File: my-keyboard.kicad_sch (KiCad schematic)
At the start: 156 parts, among them SW1 SW_Push, U1 ATmega32U4-AU, Y1 16MHz

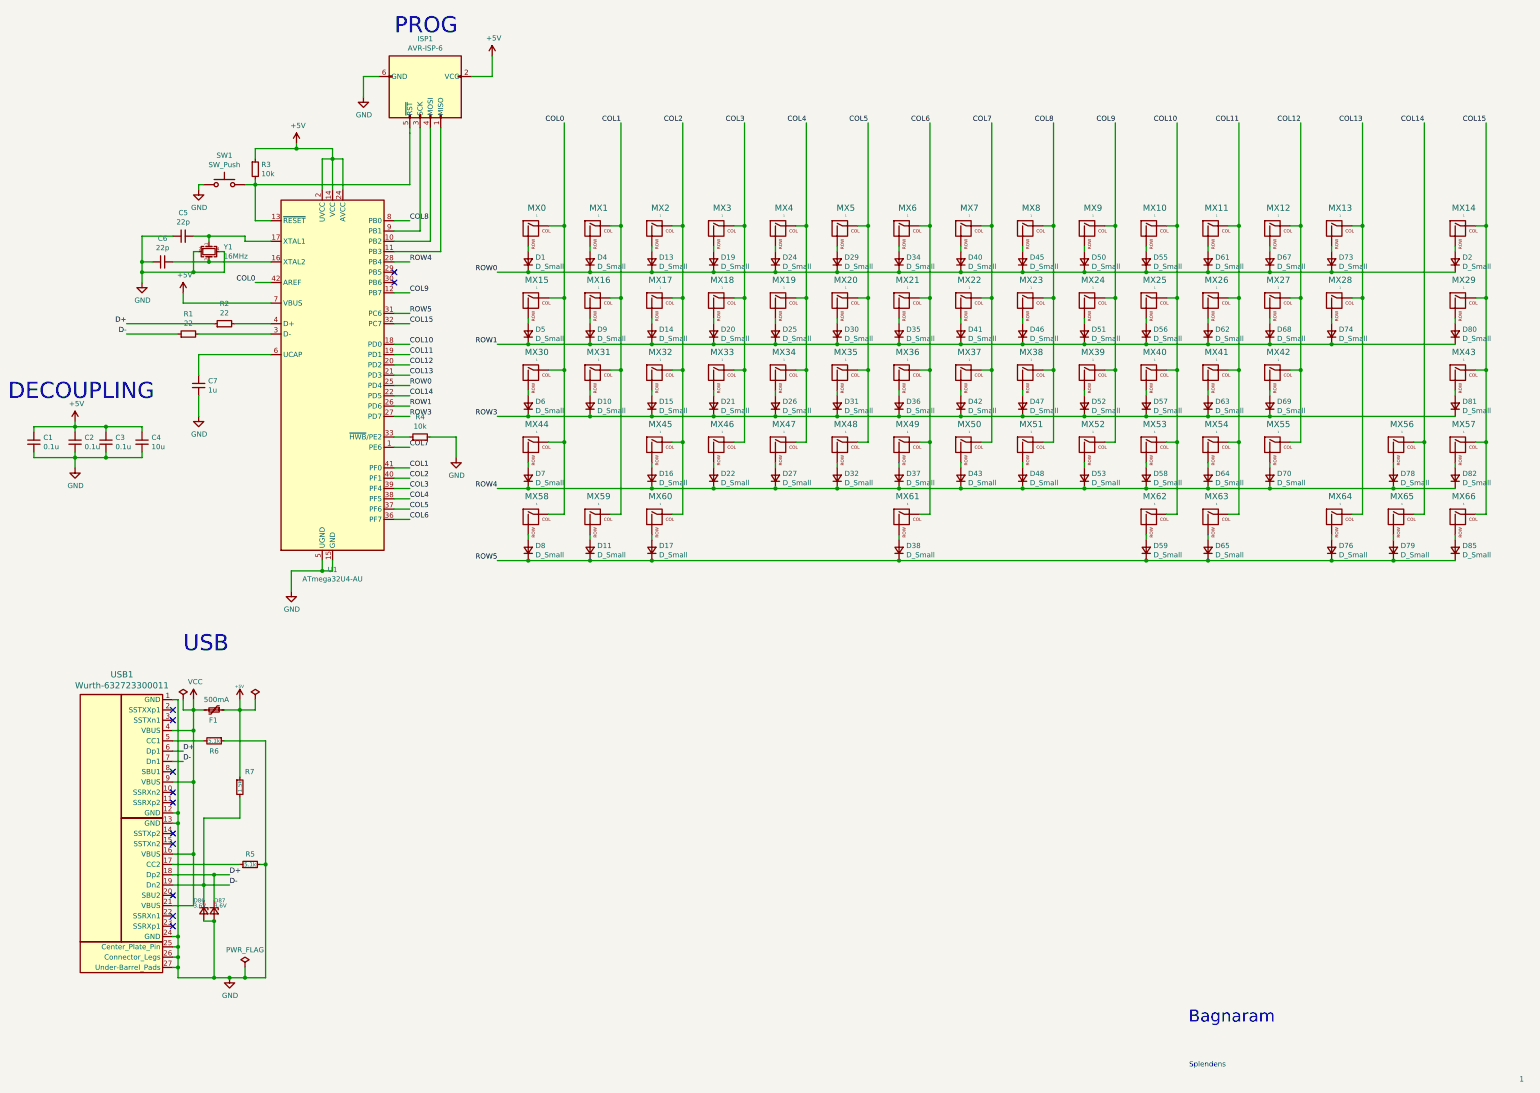
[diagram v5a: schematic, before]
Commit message: fix aref pin
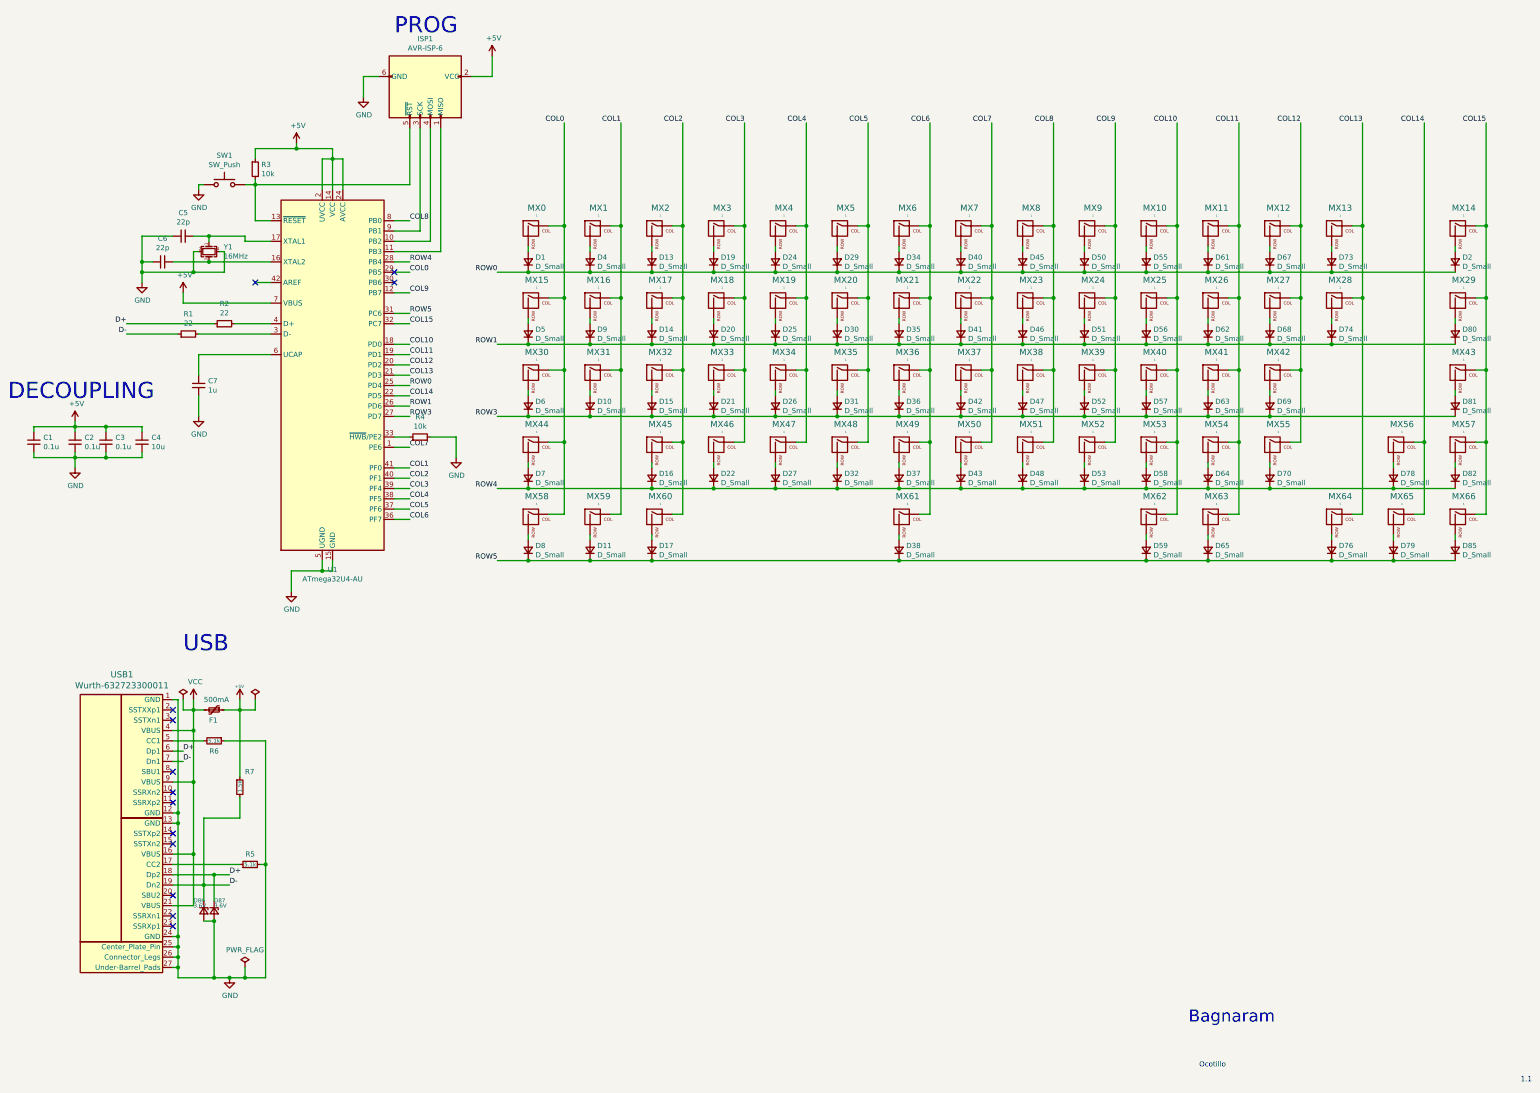
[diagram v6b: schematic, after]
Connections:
- net COL0: now also U1.29 (PB5); no longer U1.42 (AREF)
- no-connect marks 12 -> 13
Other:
- note added: "1.1"
- note added: "Ocotillo"
- note removed: "1"
- note removed: "Splendens"
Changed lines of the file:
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@@
   (junction (at 383.54 105.41) (diameter 1.016) (color 0 0 0 0))
   (junction (at 383.54 123.19) (diameter 1.016) (color 0 0 0 0))
-  (no_connect (at 59.69 234.95))
+  (no_connect (at 59.69 204.47))
   (no_connect (at 59.69 212.09))
-  (no_connect (at 59.69 219.71))
-  (no_connect (at 59.69 242.57))
-  (no_connect (at 59.69 191.77))
+  (no_connect (at 80.01 83.82))
   (no_connect (at 59.69 222.25))
   (no_connect (at 114.3 81.28))
-  (no_connect (at 59.69 204.47))
+  (no_connect (at 59.69 191.77))
+  (no_connect (at 59.69 219.71))
+  (no_connect (at 59.69 240.03))
+  (no_connect (at 59.69 242.57))
+  (no_connect (at 59.69 209.55))
+  (no_connect (at 59.69 234.95))
   (no_connect (at 59.69 189.23))
-  (no_connect (at 59.69 240.03))
   (no_connect (at 114.3 83.82))
-  (no_connect (at 59.69 209.55))
   (wire (pts (xy 25.4 119.38) (xy 25.4 120.65))
     (stroke (width 0) (type solid) (color 0 0 0 0))
@@
     (stroke (width 0) (type solid) (color 0 0 0 0))
   )
+  (wire (pts (xy 114.3 81.28) (xy 118.11 81.28))
+    (stroke (width 0) (type solid) (color 0 0 0 0))
+  )
   (wire (pts (xy 114.3 86.36) (xy 118.11 86.36))
     (stroke (width 0) (type solid) (color 0 0 0 0))
@@
     (stroke (width 0) (type solid) (color 0 0 0 0))
   )
-  (wire (pts (xy 118.11 46.99) (xy 118.11 45.72))
-    (stroke (width 0) (type solid) (color 0 0 0 0))
-  )
-  (wire (pts (xy 118.11 46.99) (xy 118.11 59.69))
+  (wire (pts (xy 118.11 45.72) (xy 118.11 59.69))
     (stroke (width 0) (type solid) (color 0 0 0 0))
   )
@@
     (effects (font (size 3.988 3.988)) (justify left bottom))
   )
-  (text "Splendens" (at 319.3641 277.5367 180)
+  (text "Ocotillo" (at 319.3641 277.5367 180)
     (effects (font (size 1.27 1.27)) (justify right bottom))
   )
@@
     (effects (font (size 2.997 2.997)) (justify right bottom))
   )
-  (text "1" (at 392.8618 281.2542 180)
+  (text "1.1" (at 394.8263 281.2219 180)
     (effects (font (size 1.27 1.27)) (justify right bottom))
   )
@@
     (effects (font (size 1.27 1.27)) (justify left bottom))
   )
-  (label "COL0" (at 80.01 83.82 180)
-    (effects (font (size 1.27 1.27)) (justify right bottom))
-  )
   (label "COL8" (at 118.11 68.58 0)
     (effects (font (size 1.27 1.27)) (justify left bottom))
@@
     (effects (font (size 1.27 1.27)) (justify left bottom))
   )
+  (label "COL0" (at 118.11 81.28 0)
+    (effects (font (size 1.27 1.27)) (justify left bottom))
+  )
